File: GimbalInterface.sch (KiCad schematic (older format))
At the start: 1 part

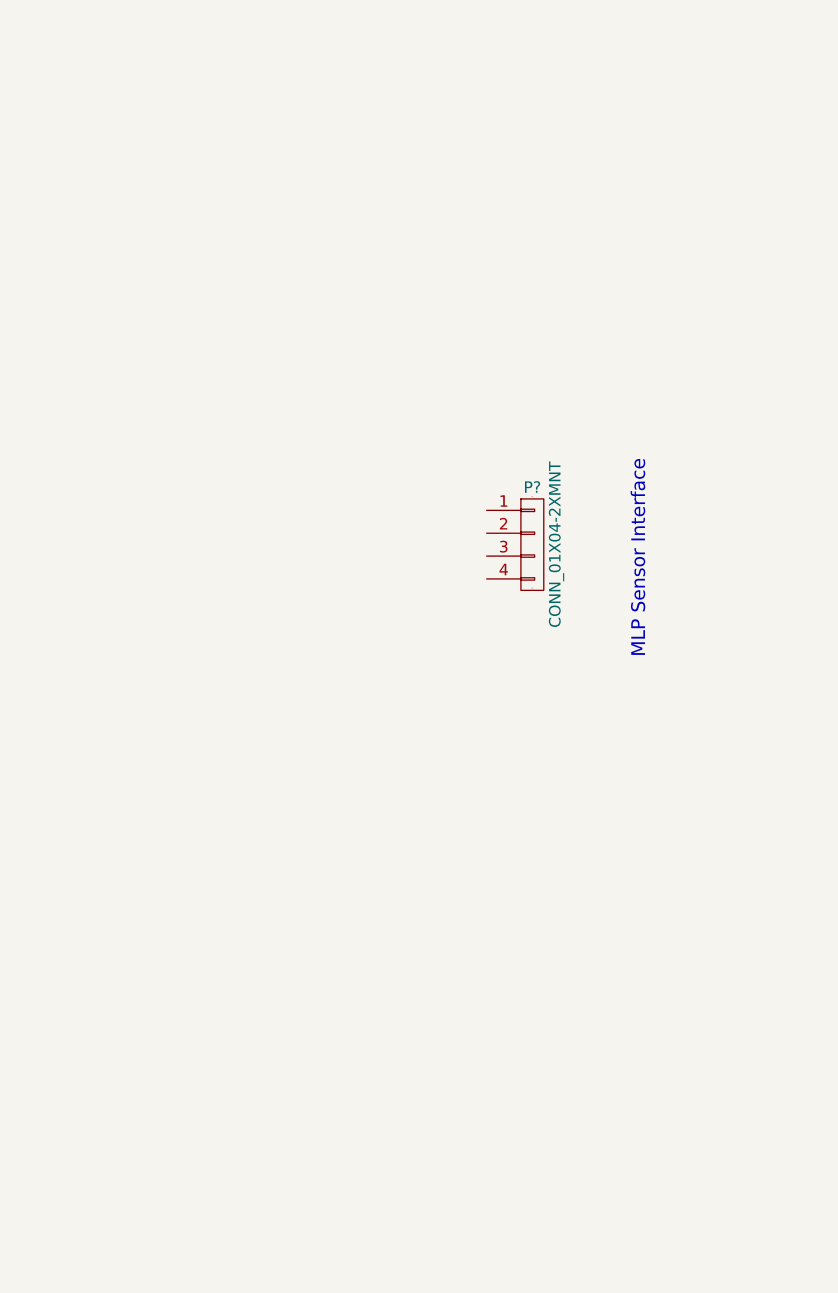
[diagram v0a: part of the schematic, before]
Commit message: Place basic parts.
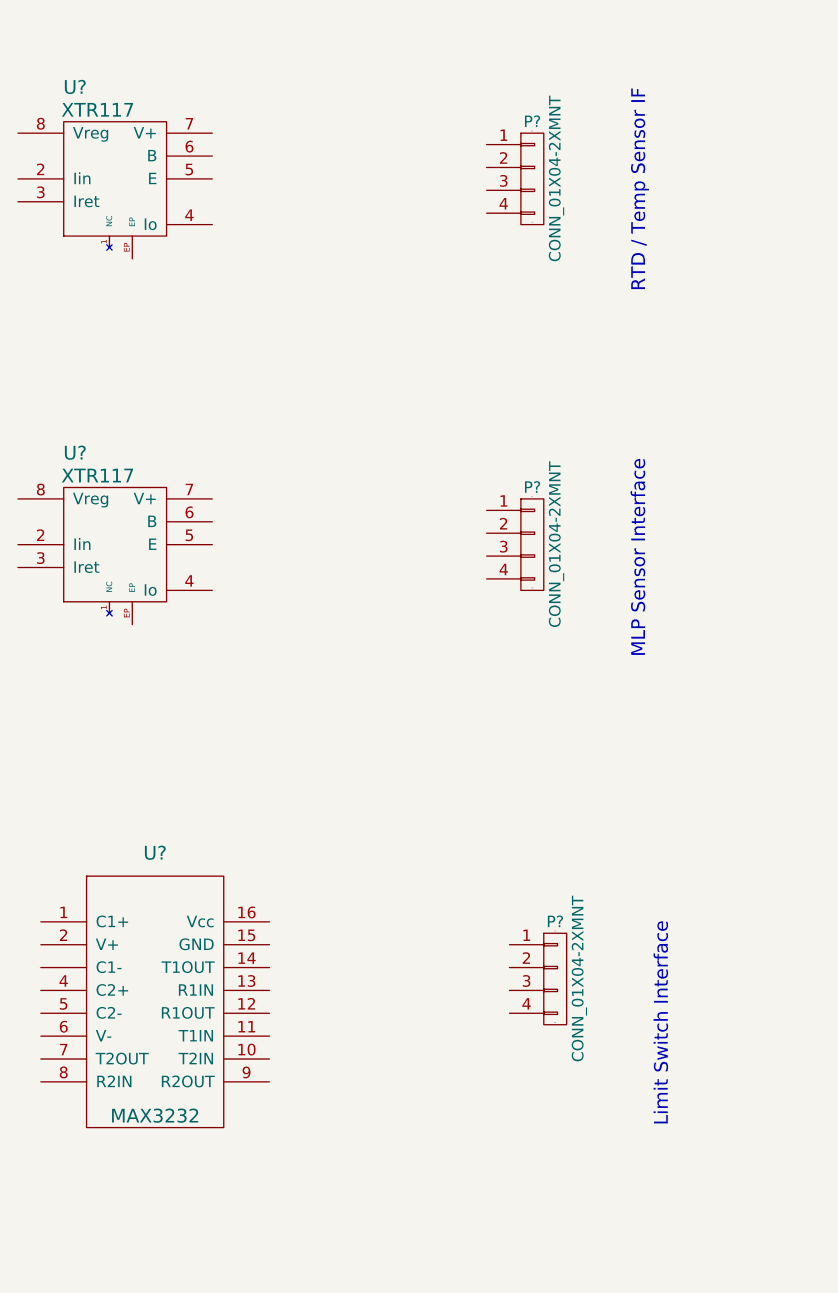
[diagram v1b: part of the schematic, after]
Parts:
- added P? (x2): CONN_01X04-2XMNT, symbol CONN_01X04-2XMNT
- added U? (x2): XTR117, symbol XTR117
- added U?: MAX3232, symbol MAX3232
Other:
- note added: "Limit Switch Interface"
- note added: "RTD / Temp Sensor IF"
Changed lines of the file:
@@
 Text Notes 13250 3600 1    60   ~ 0
 MLP Sensor Interface
+$Comp
+L XTR117 U?
+U 1 1 57540473
+P 10700 2850
+F 0 "U?" H 10750 3000 60  0000 C CNN
+F 1 "XTR117" H 10850 2900 60  0000 C CNN
+F 2 "" H 10700 2850 60  0000 C CNN
+F 3 "" H 10700 2850 60  0000 C CNN
+	1    10700 2850
+	1    0    0    -1
+$EndComp
+$Comp
+L MAX3232 U?
+U 1 1 575404DC
+P 11000 5150
+F 0 "U?" H 11100 5850 60  0000 C CNN
+F 1 "MAX3232" H 11100 4700 60  0000 C CNN
+F 2 "" H 11000 5150 60  0000 C CNN
+F 3 "" H 11000 5150 60  0000 C CNN
+	1    11000 5150
+	1    0    0    -1
+$EndComp
+$Comp
+L CONN_01X04-2XMNT P?
+U 1 1 5754053F
+P 12850 5000
+F 0 "P?" H 12850 5250 50  0000 C CNN
+F 1 "CONN_01X04-2XMNT" V 12950 5000 50  0000 C CNN
+F 2 "" H 12850 5000 50  0000 C CNN
+F 3 "" H 12850 5000 50  0000 C CNN
+	1    12850 5000
+	1    0    0    -1
+$EndComp
+Text Notes 13350 5650 1    60   ~ 0
+Limit Switch Interface
+$Comp
+L CONN_01X04-2XMNT P?
+U 1 1 5754081B
+P 12750 1500
+F 0 "P?" H 12750 1750 50  0000 C CNN
+F 1 "CONN_01X04-2XMNT" V 12850 1500 50  0000 C CNN
+F 2 "" H 12750 1500 50  0000 C CNN
+F 3 "" H 12750 1500 50  0000 C CNN
+	1    12750 1500
+	1    0    0    -1
+$EndComp
+Text Notes 13250 2000 1    60   ~ 0
+RTD / Temp Sensor IF
+$Comp
+L XTR117 U?
+U 1 1 57540822
+P 10700 1250
+F 0 "U?" H 10750 1400 60  0000 C CNN
+F 1 "XTR117" H 10850 1300 60  0000 C CNN
+F 2 "" H 10700 1250 60  0000 C CNN
+F 3 "" H 10700 1250 60  0000 C CNN
+	1    10700 1250
+	1    0    0    -1
+$EndComp
 $EndSCHEMATC

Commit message: Minor update
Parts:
- removed U? (x2): XTR117, symbol XTR117
- removed U?: MAX3232, symbol MAX3232
- added C?: C_10nF_50V, RLOOP_FOOTPRINTS:rLoop_C_0603, symbol C_10nF_50V
- added P?: TE_640456-8, RLOOP_FOOTPRINTS:rLoop_TE640456-8, symbol TE_640456-8
- added Q?: MMBT3904, SOT-23, symbol MMBT3904
- added U?: XTR117AIDGKT, RLOOP_FOOTPRINTS:rLoop_MSOP8, symbol XTR117AIDGKT
- added U?: MAX3232CDR, RLOOP_FOOTPRINTS:rLoop_SOIC_16, symbol MAX3232CDR
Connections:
- net labels added: TEMP_I_NEG, TEMP_I_POS
- wire segments 0 -> 11
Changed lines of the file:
@@
 MLP Sensor Interface
-$Comp
-L XTR117 U?
-U 1 1 57540473
-P 10700 2850
-F 0 "U?" H 10750 3000 60  0000 C CNN
-F 1 "XTR117" H 10850 2900 60  0000 C CNN
-F 2 "" H 10700 2850 60  0000 C CNN
-F 3 "" H 10700 2850 60  0000 C CNN
-	1    10700 2850
-	1    0    0    -1
-$EndComp
-$Comp
-L MAX3232 U?
-U 1 1 575404DC
-P 11000 5150
-F 0 "U?" H 11100 5850 60  0000 C CNN
-F 1 "MAX3232" H 11100 4700 60  0000 C CNN
-F 2 "" H 11000 5150 60  0000 C CNN
-F 3 "" H 11000 5150 60  0000 C CNN
-	1    11000 5150
-	1    0    0    -1
-$EndComp
 $Comp
 L CONN_01X04-2XMNT P?
@@
 RTD / Temp Sensor IF
 $Comp
-L XTR117 U?
-U 1 1 57540822
-P 10700 1250
-F 0 "U?" H 10750 1400 60  0000 C CNN
-F 1 "XTR117" H 10850 1300 60  0000 C CNN
-F 2 "" H 10700 1250 60  0000 C CNN
-F 3 "" H 10700 1250 60  0000 C CNN
-	1    10700 1250
+L TE_640456-8 P?
+U 1 1 575B773F
+P 2450 5850
+F 0 "P?" H 2500 5900 50  0000 C CNN
+F 1 "TE_640456-8" V 2600 5450 50  0000 C CNN
+F 2 "RLOOP_FOOTPRINTS:rLoop_TE640456-8" H 2500 5450 50  0001 C CNN
+F 3 "" H 2500 5450 50  0000 C CNN
+	1    2450 5850
+	-1   0    0    -1
+$EndComp
+$Comp
+L XTR117AIDGKT U?
+U 1 1 575B8098
+P 9050 1200
+F 0 "U?" H 9100 1350 60  0000 C CNN
+F 1 "XTR117AIDGKT" H 9350 1250 60  0000 C CNN
+F 2 "RLOOP_FOOTPRINTS:rLoop_MSOP8" H 9000 1250 60  0001 C CNN
+F 3 "" H 9050 1200 60  0000 C CNN
+	1    9050 1200
 	1    0    0    -1
 $EndComp
+$Comp
+L MMBT3904 Q?
+U 1 1 575B9702
+P 10400 1450
+F 0 "Q?" H 10600 1525 50  0000 L CNN
+F 1 "MMBT3904" H 10600 1450 50  0000 L CNN
+F 2 "SOT-23" H 10600 1375 50  0000 L CIN
+F 3 "" H 10400 1450 50  0000 L CNN
+	1    10400 1450
+	1    0    0    -1
+$EndComp
+Wire Wire Line
+	9700 1250 11700 1250
+Wire Wire Line
+	9700 1350 10100 1350
+Wire Wire Line
+	10100 1350 10100 1450
+Wire Wire Line
+	10100 1450 10200 1450
+Wire Wire Line
+	9700 1450 10000 1450
+Wire Wire Line
+	10000 1450 10000 1650
+Wire Wire Line
+	10000 1650 10500 1650
+Wire Wire Line
+	9700 1650 9700 1850
+Wire Wire Line
+	9700 1850 11700 1850
+Text Label 11200 1850 0    60   ~ 0
+TEMP_I_NEG
+Text Label 11200 1250 0    60   ~ 0
+TEMP_I_POS
+$Comp
+L C_10nF_50V C?
+U 1 1 575B9CF9
+P 11100 1500
+F 0 "C?" H 11125 1600 50  0000 L CNN
+F 1 "C_10nF_50V" H 11125 1400 50  0000 L CNN
+F 2 "RLOOP_FOOTPRINTS:rLoop_C_0603" H 11138 1350 50  0001 C CNN
+F 3 "" H 11100 1500 50  0000 C CNN
+	1    11100 1500
+	1    0    0    -1
+$EndComp
+Wire Wire Line
+	11100 1350 11100 1250
+Connection ~ 11100 1250
+Wire Wire Line
+	11100 1650 11100 1850
+Connection ~ 11100 1850
+$Comp
+L MAX3232CDR U?
+U 1 1 575BA13E
+P 9700 4650
+F 0 "U?" H 10700 4750 60  0000 C CNN
+F 1 "MAX3232CDR" H 10550 2950 60  0000 C CNN
+F 2 "RLOOP_FOOTPRINTS:rLoop_SOIC_16" H 9900 4050 60  0001 C CNN
+F 3 "" H 9900 4050 60  0000 C CNN
+	1    9700 4650
+	-1   0    0    -1
+$EndComp
 $EndSCHEMATC
